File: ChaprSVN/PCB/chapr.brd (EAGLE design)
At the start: 30 parts, among them M2 RN42 Module, T1 3906, T2 3904

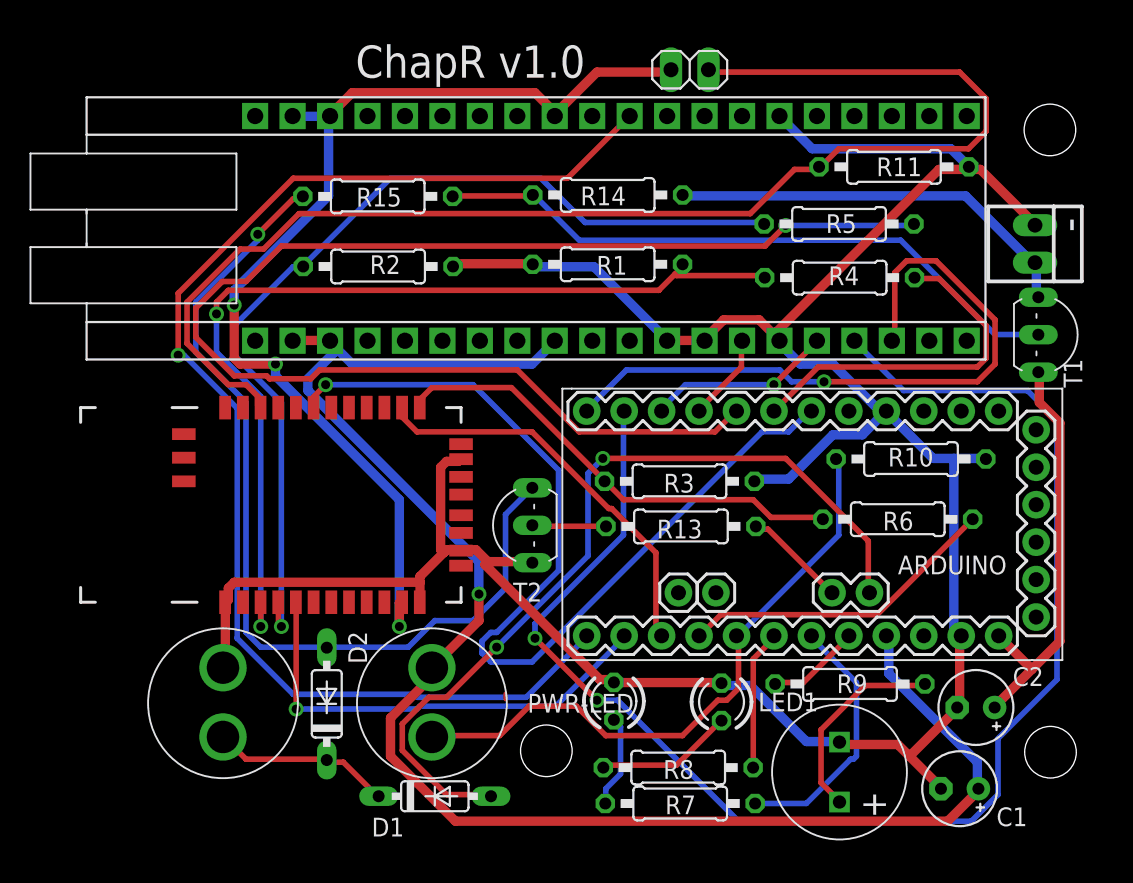
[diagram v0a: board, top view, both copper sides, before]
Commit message: Added power monitoring resistors. Fixed R15 label. Bumped to v1.1
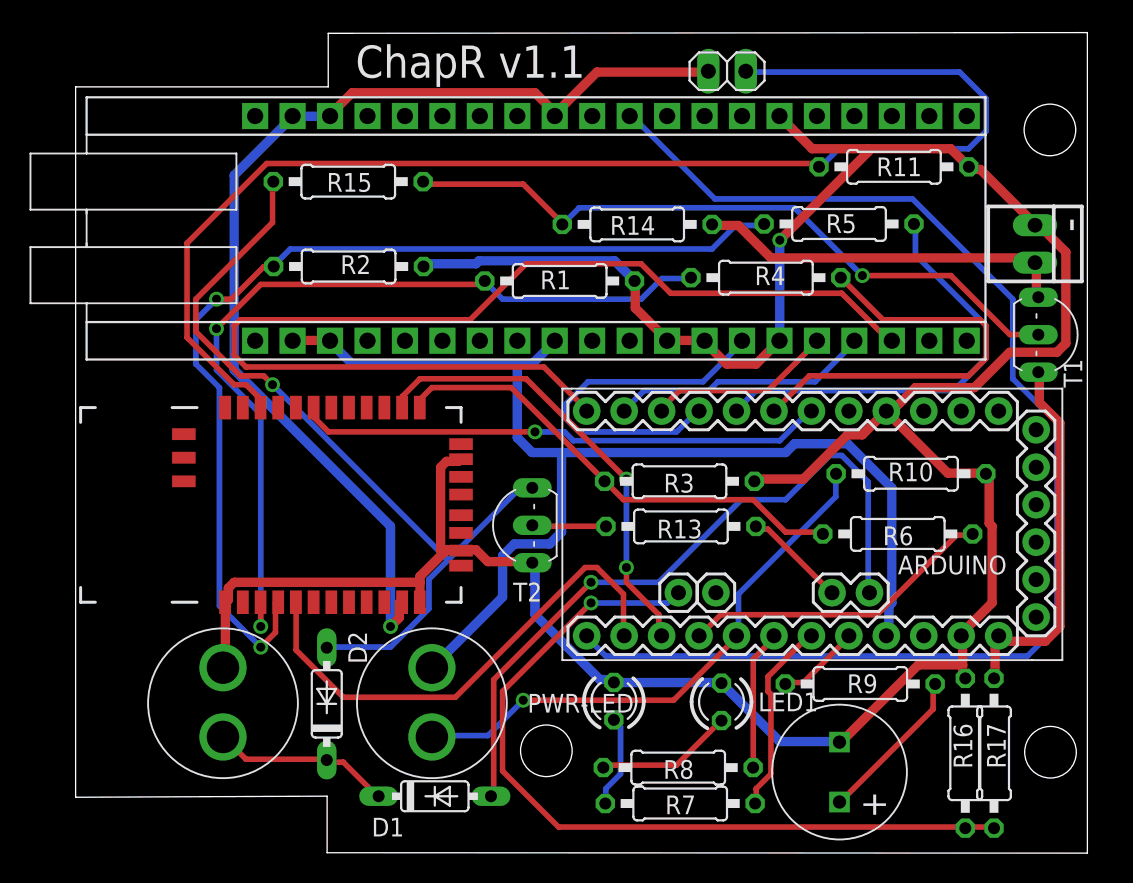
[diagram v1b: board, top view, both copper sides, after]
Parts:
- removed C1, C2: (no value), resistor:E2,5-5
- added R16, R17: 24K, resistor:0207/10
- R15: value 10k -> 1.5k
- moved R4 5.00 mm to (48.9, 39.7)
- moved R1 3.45 mm to (34.9, 39.4), turned to 180 degrees
- moved R14 2.83 mm to (40.1, 43.3)
- moved JP1 2.53 mm to (46.2, 53.7)
- moved R15 2.24 mm to (20.5, 46.2)
- moved R2 2.00 mm to (20.6, 40.4)
- moved R10 1.00 mm to (58.7, 26.4)
- moved R6 1.00 mm to (57.8, 22.3)
- moved R9 0.70 mm to (55.3, 12.1)
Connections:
- new net N$31: ARDUINO.A6, R16.1, R17.2
- net +5V: no longer C1.+
- net GND: now also R16.2; no longer C1.-, C2.-
- net N$23: now also R17.1; no longer C2.+
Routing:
- net N$11: track 98.3 -> 17.7 mm, vias 2 -> 0
- net N$8: track 93.5 -> 29.6 mm, vias 1 -> 0
- net N$31: track 0.00 -> 55.1 mm, vias 0 -> 1
- net N$10: track 46.3 -> 76.0 mm, vias 1 -> 0
- net +5V: track 111.0 -> 81.3 mm, vias 1 -> 0
- net N$15: track 64.5 -> 35.9 mm
- net N$13: track 5.95 -> 24.8 mm
- net N$29: track 57.3 -> 48.0 mm, vias 2 -> 1
- net GND: track 189.0 -> 197.7 mm, vias 0 -> 1
- net N$25: track 61.6 -> 55.4 mm
- net N$6: track 63.8 -> 57.7 mm
- net N$24: track 42.4 -> 37.4 mm, vias 0 -> 1
- net N$14: track 24.3 -> 29.3 mm
- net N$18: track 17.6 -> 13.3 mm
- net N$7: track 64.8 -> 68.9 mm, vias 1 -> 2
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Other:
- board outline added: 68.6 x 55.6 mm
- board text added: "ChapR v1.1"
- board text removed: "ChapR v1.0"
